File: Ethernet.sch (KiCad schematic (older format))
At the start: 34 parts, among them J8 RJ45_Abracon_ARJP11A-MASA-B-A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, U4 LAN8742A-CZ-TR, U5 USBLC6-4SC6, Y2 25M

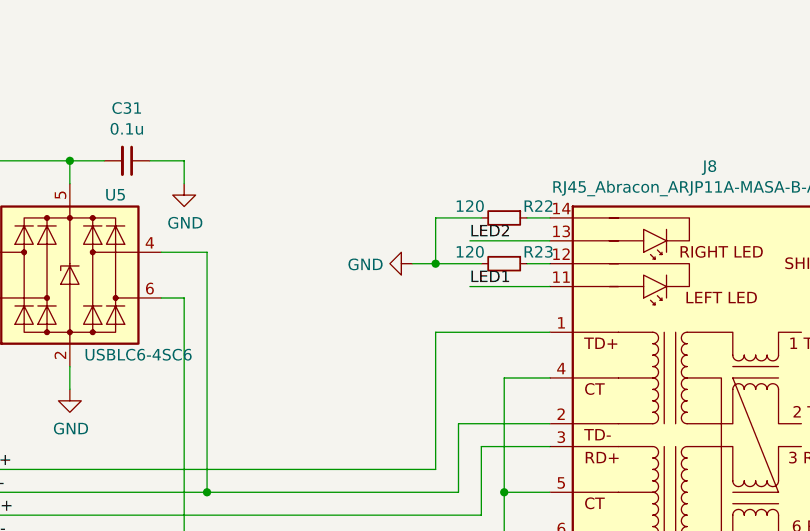
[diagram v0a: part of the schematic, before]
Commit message: adds necessary resistors, keep out zones, and TVS diode
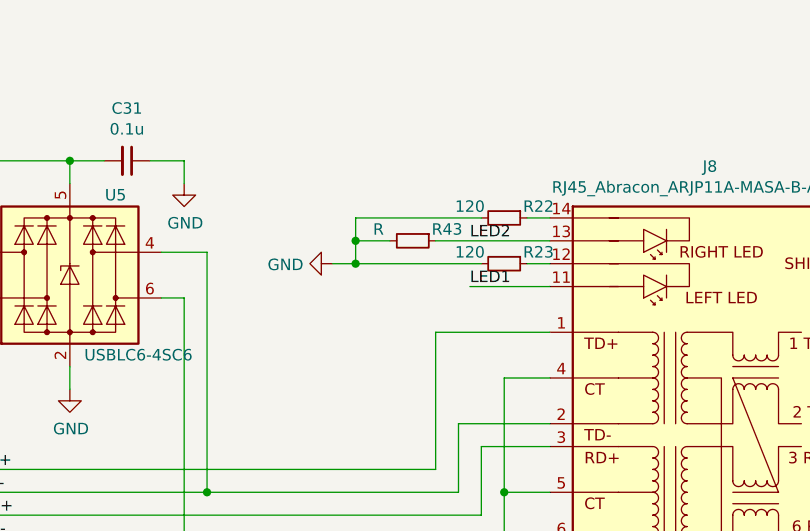
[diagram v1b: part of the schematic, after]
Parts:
- added R43: R, Resistor_SMD:R_0805_2012Metric, symbol Device:R_Small
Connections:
- net GND: now also R43.2
- net LED2: now also R43.1
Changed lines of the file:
@@
 EESchema Schematic File Version 4
-LIBS:Telemetry-Primary-cache
-EELAYER 26 0
+EELAYER 30 0
 EELAYER END
 $Descr A4 11693 8268
@@
 	1    0    0    -1
 $EndComp
-Wire Wire Line
-	9200 2550 8850 2550
 Text Label 8850 2550 0    50   ~ 0
 LED1
-Wire Wire Line
-	9200 2350 8850 2350
 Text Label 8850 2350 0    50   ~ 0
 LED2
@@
 L power:GND #PWR0146
 U 1 1 5FADEDE4
-P 8600 2450
-F 0 "#PWR0146" H 8600 2200 50  0001 C CNN
-F 1 "GND" V 8605 2322 50  0000 R CNN
-F 2 "" H 8600 2450 50  0001 C CNN
-F 3 "" H 8600 2450 50  0001 C CNN
-	1    8600 2450
+P 8250 2450
+F 0 "#PWR0146" H 8250 2200 50  0001 C CNN
+F 1 "GND" V 8255 2322 50  0000 R CNN
+F 2 "" H 8250 2450 50  0001 C CNN
+F 3 "" H 8250 2450 50  0001 C CNN
+	1    8250 2450
 	0    1    1    0
 $EndComp
@@
 $EndComp
 Wire Wire Line
-	8900 2450 8700 2450
-Wire Wire Line
-	8700 2450 8700 2250
-Wire Wire Line
-	8700 2250 8900 2250
-Wire Wire Line
-	8700 2450 8600 2450
-Connection ~ 8700 2450
+	8350 2450 8350 2350
+Wire Wire Line
+	8350 2450 8250 2450
+Connection ~ 8350 2450
 Wire Wire Line
 	8700 2750 9200 2750
@@
 Text Label 6700 3650 0    50   ~ 0
 RX-
+$Comp
+L Device:R_Small R43
+U 1 1 615D3617
+P 8600 2350
+F 0 "R43" V 8550 2500 50  0000 C CNN
+F 1 "R" V 8550 2200 50  0000 C CNN
+F 2 "Resistor_SMD:R_0805_2012Metric" V 8530 2350 50  0001 C CNN
+F 3 "~" H 8600 2350 50  0001 C CNN
+	1    8600 2350
+	0    1    1    0
+$EndComp
+Wire Wire Line
+	8350 2250 8900 2250
+Wire Wire Line
+	8350 2450 8900 2450
+Wire Wire Line
+	8700 2350 9200 2350
+Wire Wire Line
+	9200 2550 8850 2550
+Wire Wire Line
+	8500 2350 8350 2350
+Connection ~ 8350 2350
+Wire Wire Line
+	8350 2350 8350 2250
 $EndSCHEMATC

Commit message: Adds phy resistors and moves power conn away from recom
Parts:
- added R44: R, Resistor_SMD:R_0805_2012Metric, symbol Device:R
- J8: symbol Telemetry-Primary-rescue:RJ45_Abracon_ARJP11A-MASA-B-A-EMU2-Connector -> Telemetry-Primary-rescue:RJ45_Abracon_ARJP11A-MASA-B-A-EMU2-Connector-Telemetry-Primary-rescue
- U4: symbol utsvt-chips:LAN8742A-CZ-TR -> Telemetry-Primary-rescue:LAN8742A-CZ-TR-utsvt-chips
- U5: symbol Telemetry-Primary-rescue:USBLC6-4SC6-Power_Protection -> Telemetry-Primary-rescue:USBLC6-4SC6-Power_Protection-Telemetry-Primary-rescue
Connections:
- net TX+: now also R44.1
- net at C29.2, C30.2, C31.2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: now also R44.2
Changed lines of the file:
@@
 $EndDescr
 $Comp
-L Telemetry-Primary-rescue:USBLC6-4SC6-Power_Protection U5
+L Telemetry-Primary-rescue:USBLC6-4SC6-Power_Protection-Telemetry-Primary-rescue U5
 U 1 1 5F8F389F
 P 7100 2500
@@
 $EndComp
 $Comp
-L utsvt-chips:LAN8742A-CZ-TR U4
+L Telemetry-Primary-rescue:LAN8742A-CZ-TR-utsvt-chips U4
 U 1 1 5F8F7D15
 P 3800 3250
@@
 $EndComp
 $Comp
-L Telemetry-Primary-rescue:RJ45_Abracon_ARJP11A-MASA-B-A-EMU2-Connector J8
+L Telemetry-Primary-rescue:RJ45_Abracon_ARJP11A-MASA-B-A-EMU2-Connector-Telemetry-Primary-rescue J8
 U 1 1 5FA4E03B
 P 9900 3550
@@
 	7800 4350 8200 4350
 $Comp
-L Telemetry-Primary-rescue:GND2-power #PWR0145
+L Telemetry-Primary-rescue:GND2-power-Telemetry-Primary-rescue #PWR0145
 U 1 1 5FA6BA5E
 P 10700 2550
@@
 	9200 3250 8900 3250
 Wire Wire Line
-	6600 3350 8700 3350
+	6600 3350 8200 3350
 Wire Wire Line
 	8700 3350 8700 2750
@@
 Wire Wire Line
 	8350 2350 8350 2250
+$Comp
+L Device:R R44
+U 1 1 615AE01D
+P 8200 4000
+F 0 "R44" H 8270 4046 50  0000 L CNN
+F 1 "R" H 8270 3955 50  0000 L CNN
+F 2 "Resistor_SMD:R_0805_2012Metric" V 8130 4000 50  0001 C CNN
+F 3 "~" H 8200 4000 50  0001 C CNN
+	1    8200 4000
+	1    0    0    -1
+$EndComp
+Wire Wire Line
+	8200 3350 8200 3850
+Connection ~ 8200 3350
+Wire Wire Line
+	8200 3350 8700 3350
+Wire Wire Line
+	8200 4150 8200 4350
 $EndSCHEMATC

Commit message: Minor adjustments
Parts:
- removed R44: R, Resistor_SMD:R_0805_2012Metric, symbol Device:R
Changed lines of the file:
@@
 	9200 3250 8900 3250
-Wire Wire Line
-	6600 3350 8200 3350
 Wire Wire Line
 	8700 3350 8700 2750
@@
 Wire Wire Line
 	8350 2350 8350 2250
-$Comp
-L Device:R R44
-U 1 1 615AE01D
-P 8200 4000
-F 0 "R44" H 8270 4046 50  0000 L CNN
-F 1 "R" H 8270 3955 50  0000 L CNN
-F 2 "Resistor_SMD:R_0805_2012Metric" V 8130 4000 50  0001 C CNN
-F 3 "~" H 8200 4000 50  0001 C CNN
-	1    8200 4000
-	1    0    0    -1
-$EndComp
 Wire Wire Line
-	8200 3350 8200 3850
-Connection ~ 8200 3350
-Wire Wire Line
-	8200 3350 8700 3350
-Wire Wire Line
-	8200 4150 8200 4350
+	6600 3350 8700 3350
 $EndSCHEMATC
